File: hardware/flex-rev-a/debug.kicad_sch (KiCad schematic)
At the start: 0 parts

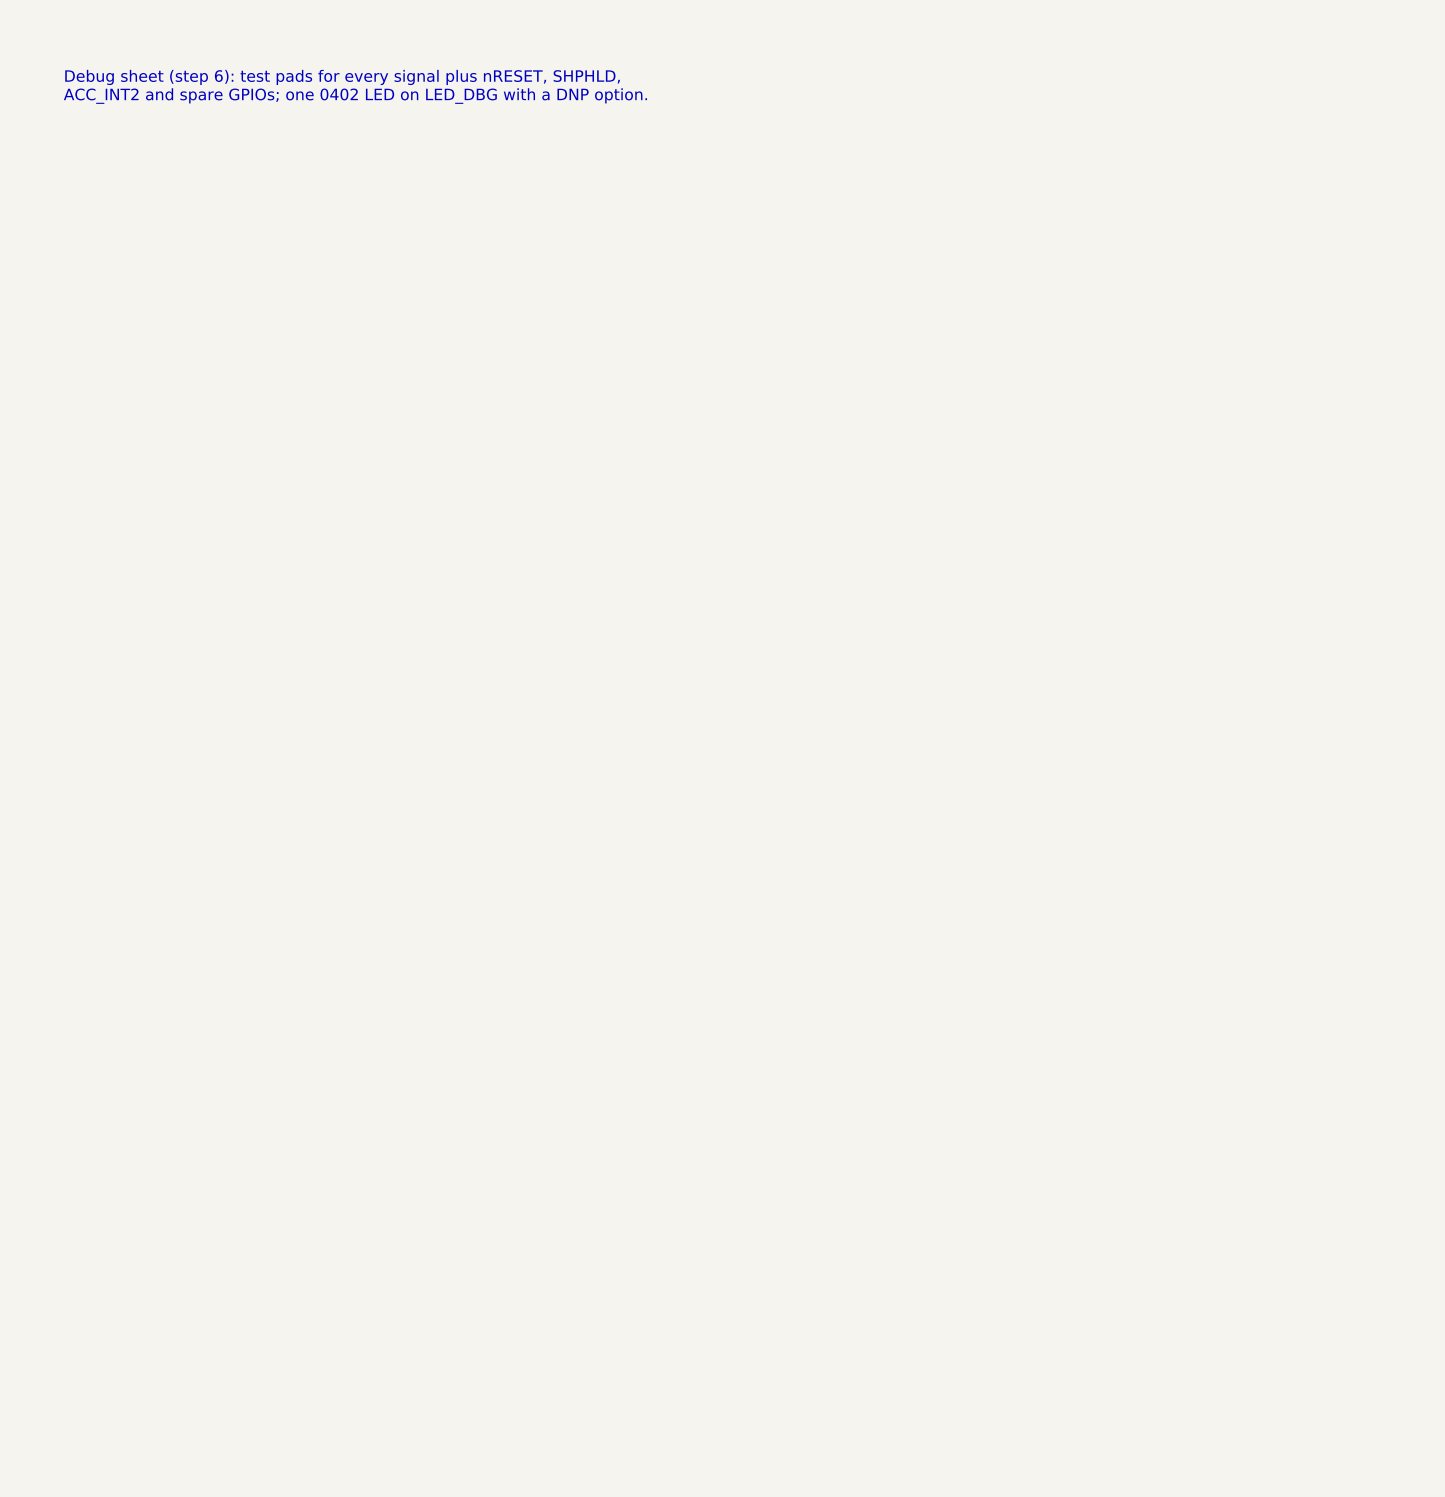
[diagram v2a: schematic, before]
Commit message: Draw debug sheet: test pads and DNP debug LED
- 0.8 mm round test pads (project footprint, no paste) on nRESET,
  I2C_SDA, I2C_SCL, VDD_1V8, VSYS, VBAT and GND. SHPHLD and ACC_INT2
  already have pads on the power and sensors sheets.
- LED_DBG -> 1k -> 0402 red LED -> GND, both DNP.
- nRESET has only a test pad (internal pull-up in the nRF54L15). The
  passive pad satisfies KiCad's "input not driven" check, so the nRESET
  error clears without an exclusion; noted on the sheet.

ERC: 0 errors, 1 warning (ISP2454 hidden VSS pins vs GND label).

Co-Authored-By: Claude Opus 5.5 <noreply@anthropic.com>
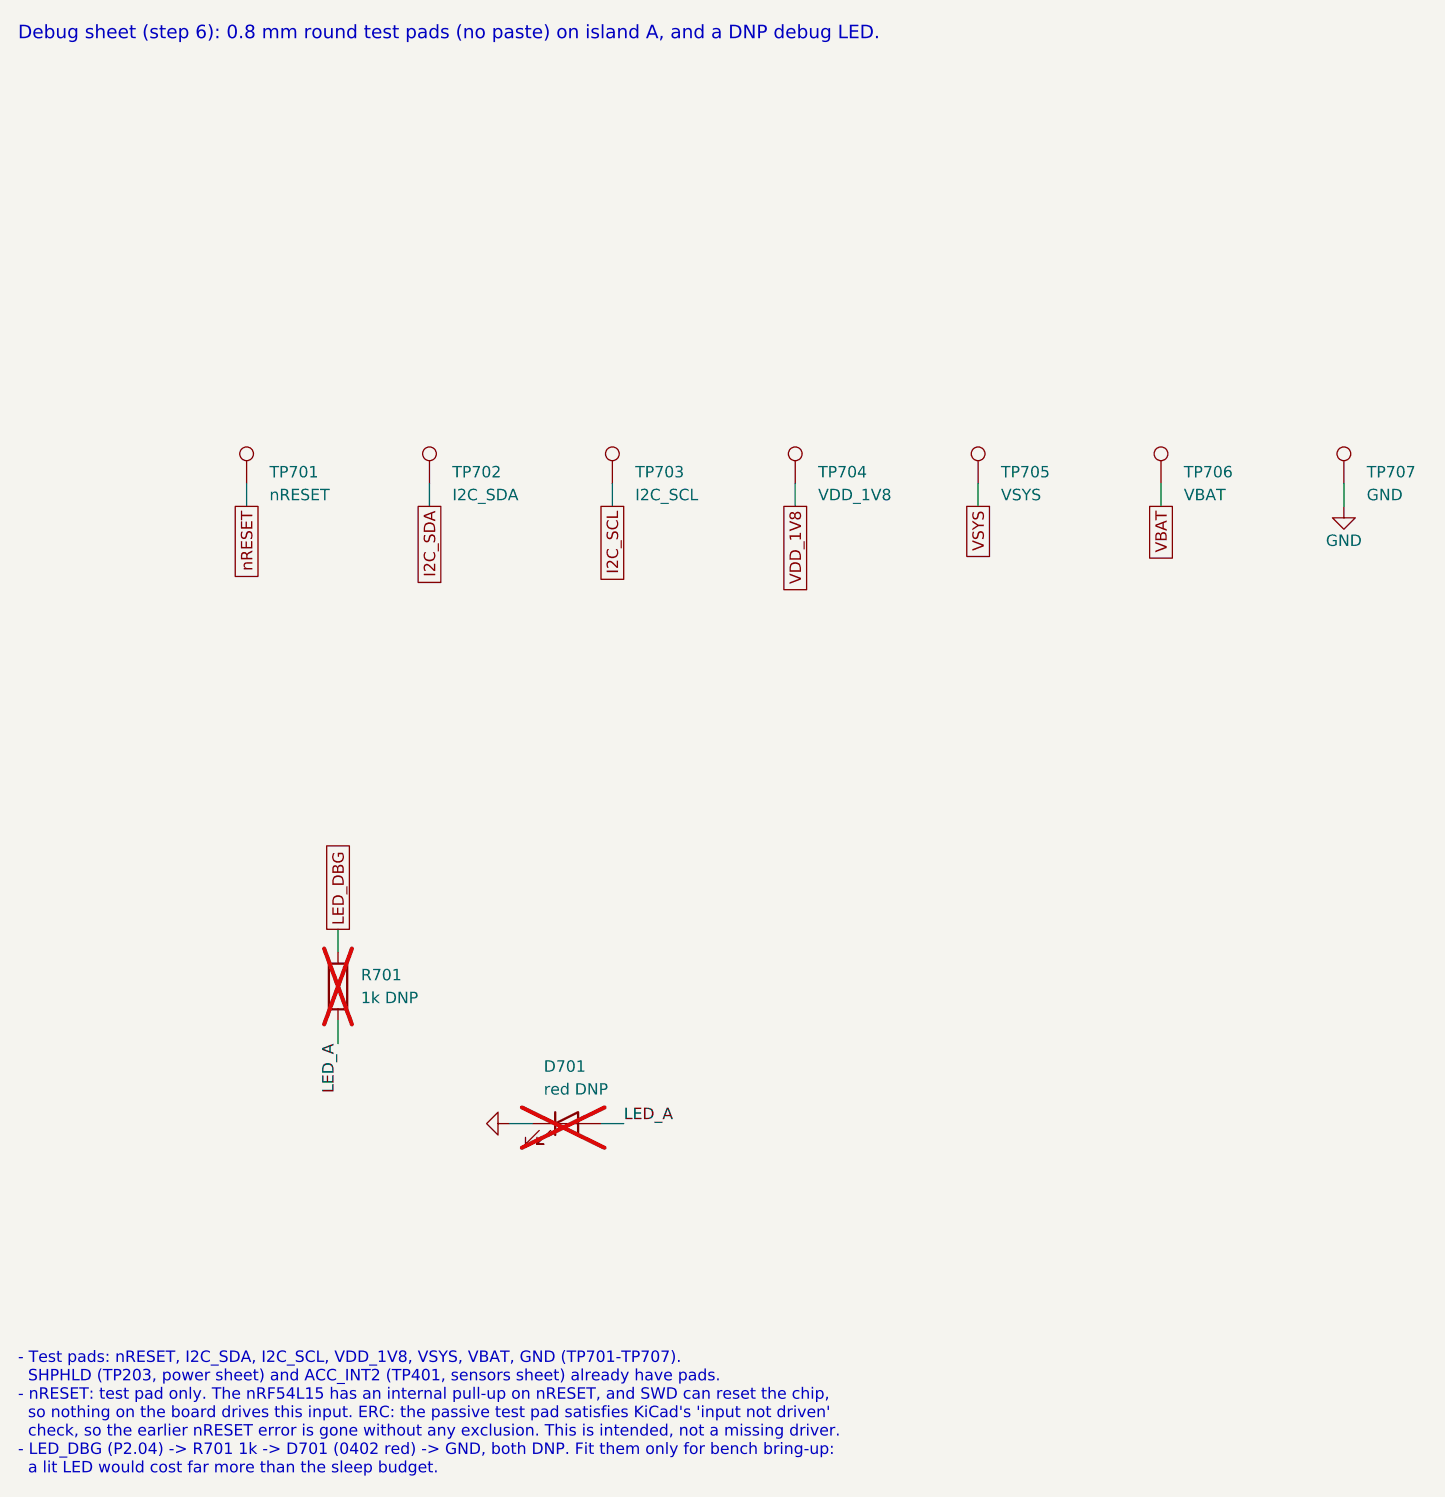
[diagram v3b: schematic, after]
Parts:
- added D701: red DNP, LED_SMD:LED_0402_1005Metric, symbol Device:LED
- added R701: 1k DNP, Resistor_SMD:R_0402_1005Metric, symbol Device:R
- added TP701: nRESET, wakeband:TestPoint_Pad_D0.8mm, symbol Connector:TestPoint
- added TP702: I2C_SDA, wakeband:TestPoint_Pad_D0.8mm, symbol Connector:TestPoint
- added TP703: I2C_SCL, wakeband:TestPoint_Pad_D0.8mm, symbol Connector:TestPoint
- added TP704: VDD_1V8, wakeband:TestPoint_Pad_D0.8mm, symbol Connector:TestPoint
- added TP705: VSYS, wakeband:TestPoint_Pad_D0.8mm, symbol Connector:TestPoint
- added TP706: VBAT, wakeband:TestPoint_Pad_D0.8mm, symbol Connector:TestPoint
- added TP707: GND, wakeband:TestPoint_Pad_D0.8mm, symbol Connector:TestPoint
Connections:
- new net GND: D701.1 (K), TP707.1
- new net I2C_SCL: TP703.1
- new net I2C_SDA: TP702.1
- new net LED_A: D701.2 (A), R701.2
- new net LED_DBG: R701.1
- new net VBAT: TP706.1
- new net VDD_1V8: TP704.1
- new net VSYS: TP705.1
- new net nRESET: TP701.1
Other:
- note added: "- Test pads: nRESET, I2C_SDA, I2C_SCL, VDD_1V8, VSYS, VBAT, GND (TP701-TP707). SHPHLD (TP203, power sheet) and ACC_INT2 (TP401, sensors sheet) already have pads. - nRESET: test pad only. The nRF54L15 has an internal pull-up on nRESET, and SWD can reset the chip, so nothing on the board drives this input. ERC: the passive test pad satisfies KiCad's 'input not driven' check, so the earlier nRESET e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"
- note added: "Debug sheet (step 6): 0.8 mm round test pads (no paste) on island A, and a DNP debug LED."
- note removed: "Debug sheet (step 6): test pads for every signal plus nRESET, SHPHLD, ACC_INT2 and spare GPIOs; one 0402 LED on LED_DBG with a DNP option."

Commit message: Apply schematic review fixes: 2.0 V rail, pad 10 NC, VIN TVS, bulk cap
- Power: R202 47k -> 68k so BUCK1 starts at 2.0 V; global net VDD_1V8
  renamed VDD_2V0 on every sheet, notes updated.
- Haptics: DRV2605L IN/TRIG tied to GND, HAPT_TRIG removed (effects run
  over I2C). Footprint kept as Package_SO:TSSOP-10_3x3mm_P0.5mm: it is
  KiCad's TI DGS land pattern (cites MPDS035); KiCad 10 has no footprint
  named VSSOP-10_3x3mm_P0.5mm.
- MCU: pad 10 (P1.10) no-connect; GND global label replaced by the GND
  power symbol; note on the trapped lower-row GND pads 12/14/16/18 and on
  pads 8/24.
- Sensors: C403 10 uF on LIS2DW12 VDD per ST; related (check) removed.
- Dock: VIN TVS is now Littelfuse SMF18A (SOD-123FL, 18 V standoff, LCSC
  C409420); data pads keep TPD1E10B06, TPD1E0B04 noted as a lower-leakage
  alternative (check).
- bom.csv regenerated, PDF replotted, README updated.

ERC: 0 errors, 0 warnings.

Co-Authored-By: Claude Opus 5.5 <noreply@anthropic.com>
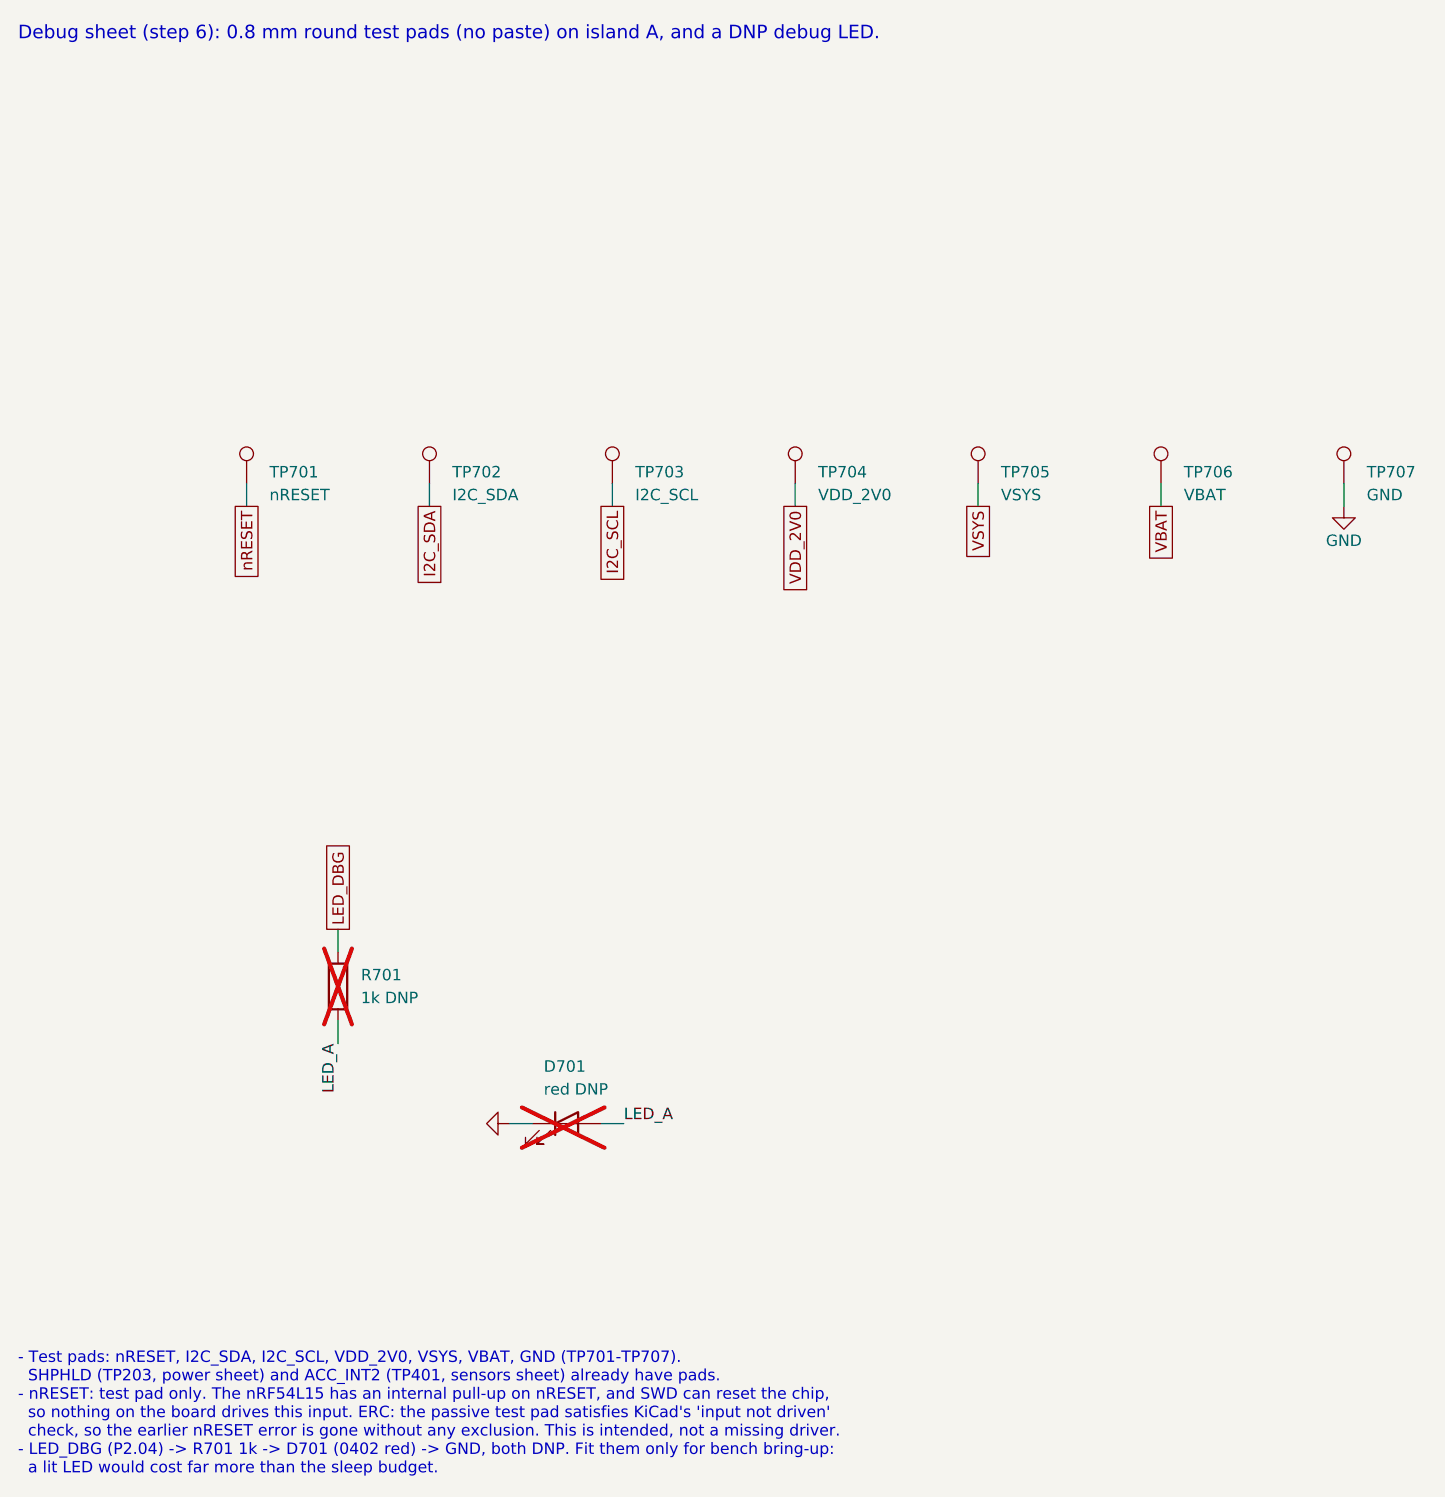
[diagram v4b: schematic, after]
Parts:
- TP704: value VDD_1V8 -> VDD_2V0
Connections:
- net VDD_1V8 renamed VDD_2V0
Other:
- note added: "- Test pads: nRESET, I2C_SDA, I2C_SCL, VDD_2V0, VSYS, VBAT, GND (TP701-TP707). SHPHLD (TP203, power sheet) and ACC_INT2 (TP401, sensors sheet) already have pads. - nRESET: test pad only. The nRF54L15 has an internal pull-up on nRESET, and SWD can reset the chip, so nothing on the board drives this input. ERC: the passive test pad satisfies KiCad's 'input not driven' check, so the earlier nRESET e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"
- note removed: "- Test pads: nRESET, I2C_SDA, I2C_SCL, VDD_1V8, VSYS, VBAT, GND (TP701-TP707). SHPHLD (TP203, power sheet) and ACC_INT2 (TP401, sensors sheet) already have pads. - nRESET: test pad only. The nRF54L15 has an internal pull-up on nRESET, and SWD can reset the chip, so nothing on the board drives this input. ERC: the passive test pad satisfies KiCad's 'input not driven' check, so the earlier nRESET e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"
